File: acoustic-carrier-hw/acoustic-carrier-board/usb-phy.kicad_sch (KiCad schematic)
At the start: 52 parts, among them J801 TYPE-C-31-M-12, U801 USB3300-EZK, U802 LMV321, Y801 Crystal_GND24_Small

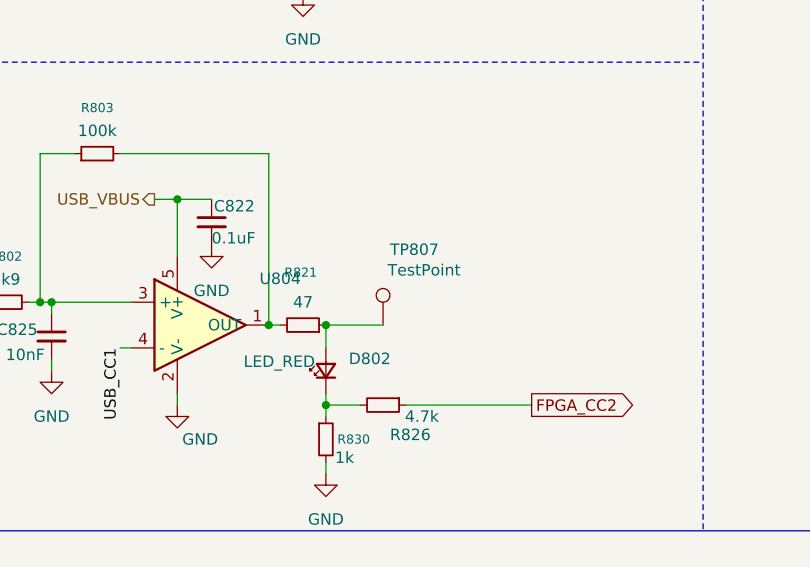
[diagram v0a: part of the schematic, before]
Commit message: [carrier] added silkscreen, moved lpddr3 traces around slightly
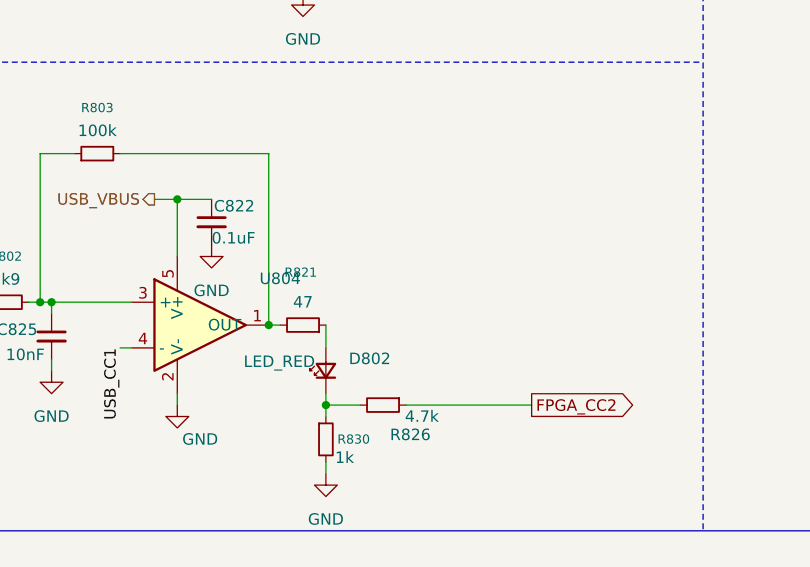
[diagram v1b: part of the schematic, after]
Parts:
- removed TP807: TestPoint, TestPoint:TestPoint_Loop_D1.80mm_Drill1.0mm_Beaded, symbol Connector:TestPoint
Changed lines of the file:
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@@
 	)
 	(junction
-		(at 288.29 224.79)
-		(diameter 0)
-		(color 0 0 0 0)
-	)
-	(junction
 		(at 279.4 172.72)
 		(diameter 0)
@@
 	(wire
 		(pts
-			(xy 288.29 224.79) (xy 294.64 224.79)
-		)
-		(stroke
-			(width 0)
-			(type default)
-		)
-	)
-	(wire
-		(pts
 			(xy 297.18 233.68) (xy 311.15 233.68)
 		)
@@
 					(unit 1)
 				)
-			)
-		)
-	)
-	(symbol
-		(lib_id "Connector:TestPoint")
-		(at 294.64 224.79 0)
-		(unit 1)
-		(exclude_from_sim no)
-		(in_bom yes)
-		(on_board yes)
-		(dnp no)
-		(property "Reference" "TP807"
-			(at 295.402 216.408 0)
-			(effects
-				(font
-					(size 1.27 1.27)
-				)
-				(justify left)
-			)
-		)
-		(property "Value" "TestPoint"
-			(at 295.148 218.694 0)
-			(effects
-				(font
-					(size 1.27 1.27)
-				)
-				(justify left)
-			)
-		)
-		(property "Footprint" "TestPoint:TestPoint_Loop_D1.80mm_Drill1.0mm_Beaded"
-			(at 299.72 224.79 0)
-			(effects
-				(font
-					(size 1.27 1.27)
-				)
-				(hide yes)
-			)
-		)
-		(property "Datasheet" "~"
-			(at 299.72 224.79 0)
-			(effects
-				(font
-					(size 1.27 1.27)
-				)
-				(hide yes)
-			)
-		)
-		(property "Description" "test point"
-			(at 294.64 224.79 0)
-			(effects
-				(font
-					(size 1.27 1.27)
-				)
-				(hide yes)
-			)
-		)
-		(pin "1"
-		)
-		(instances
-			(project "acoustic-carrier-board"
-				(path "/25b015c9-ab13-4427-b72c-b6f348597100/bccc7554-d2b1-4102-8d28-ddff56ec5c7a"
-					(reference "TP807")
-					(unit 1)
-				)

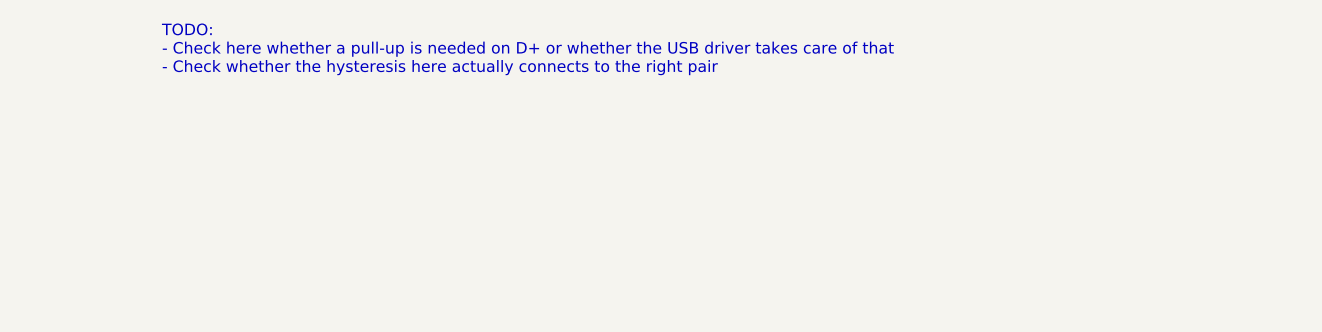
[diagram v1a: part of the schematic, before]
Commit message: [carrier] finished final review, (next) posting to linkedin, start working on analog front-end board
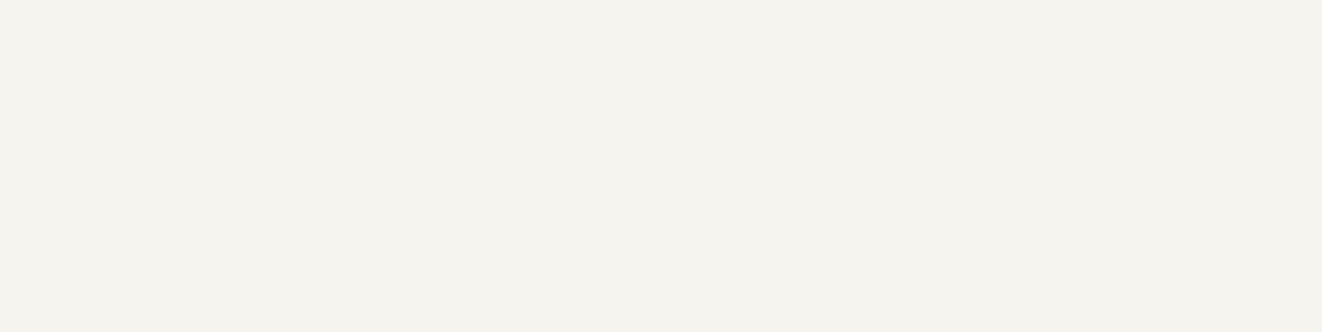
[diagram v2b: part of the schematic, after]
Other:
- note removed: "TODO: - Check here whether a pull-up is needed on D+ or whether the USB driver takes care of that - Check whether the hysteresis here actually connects to the right pair"
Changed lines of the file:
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@@
-		)
-	)
-	(text "TODO: \n- Check here whether a pull-up is needed on D+ or whether the USB driver takes care of that\n- Check whether the hysteresis here actually connects to the right pair"
-		(exclude_from_sim no)
-		(at 162.814 -21.336 0)
-		(effects
-			(font
-				(size 1.27 1.27)
-			)
-			(justify left bottom)
 		)
 	)

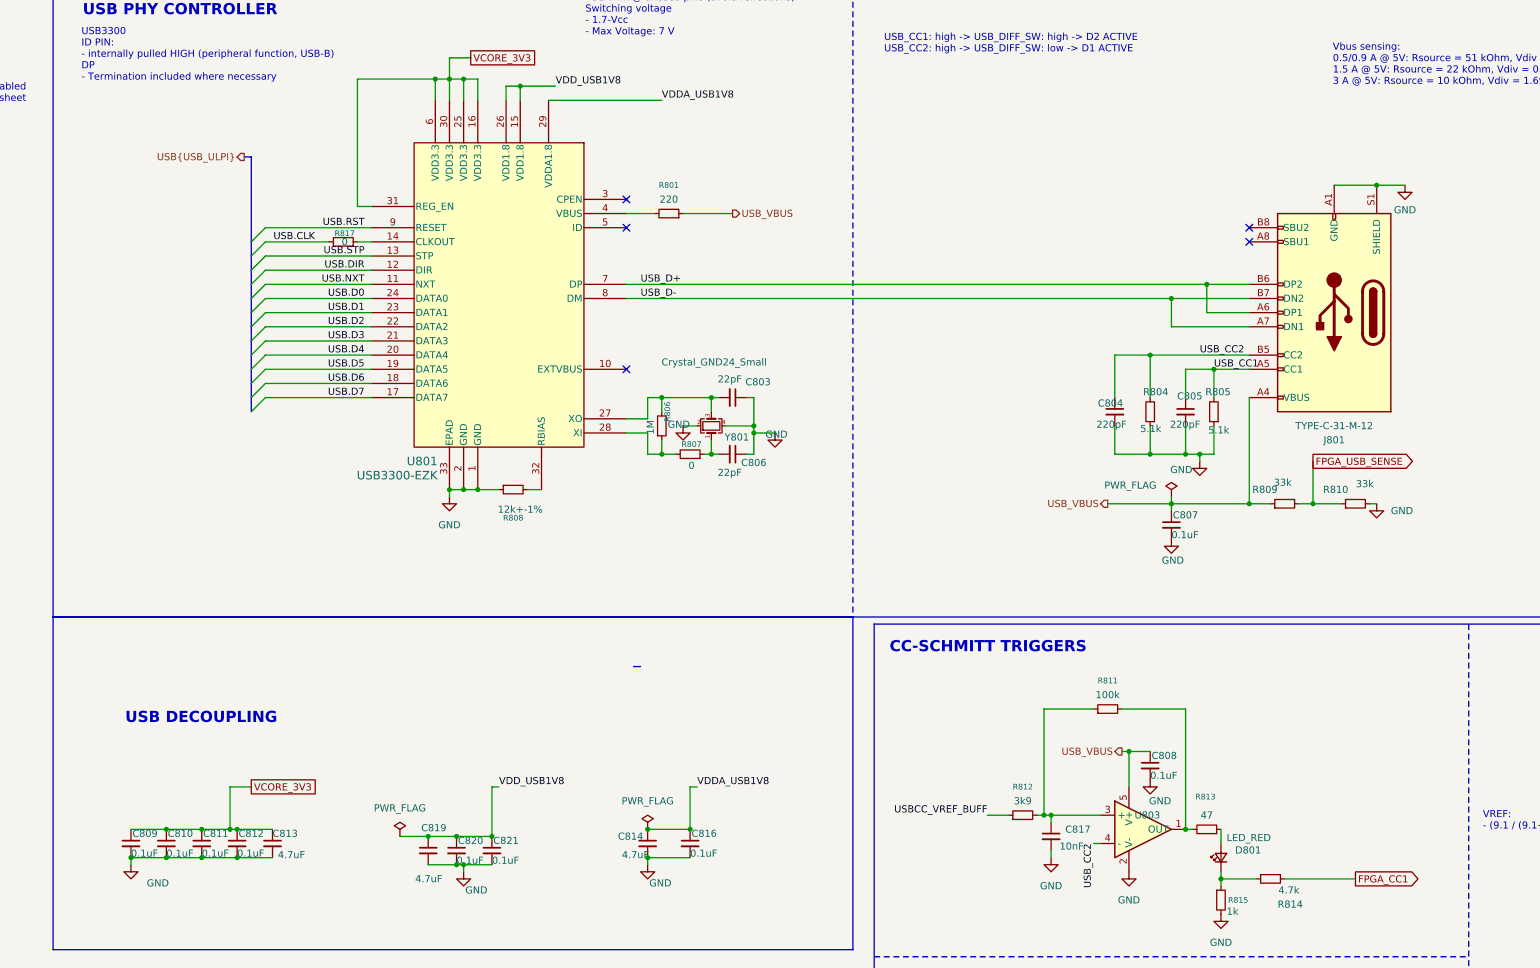
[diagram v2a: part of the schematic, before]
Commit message: [carrier] Added LC-filter between SHIELD and GND, added comments
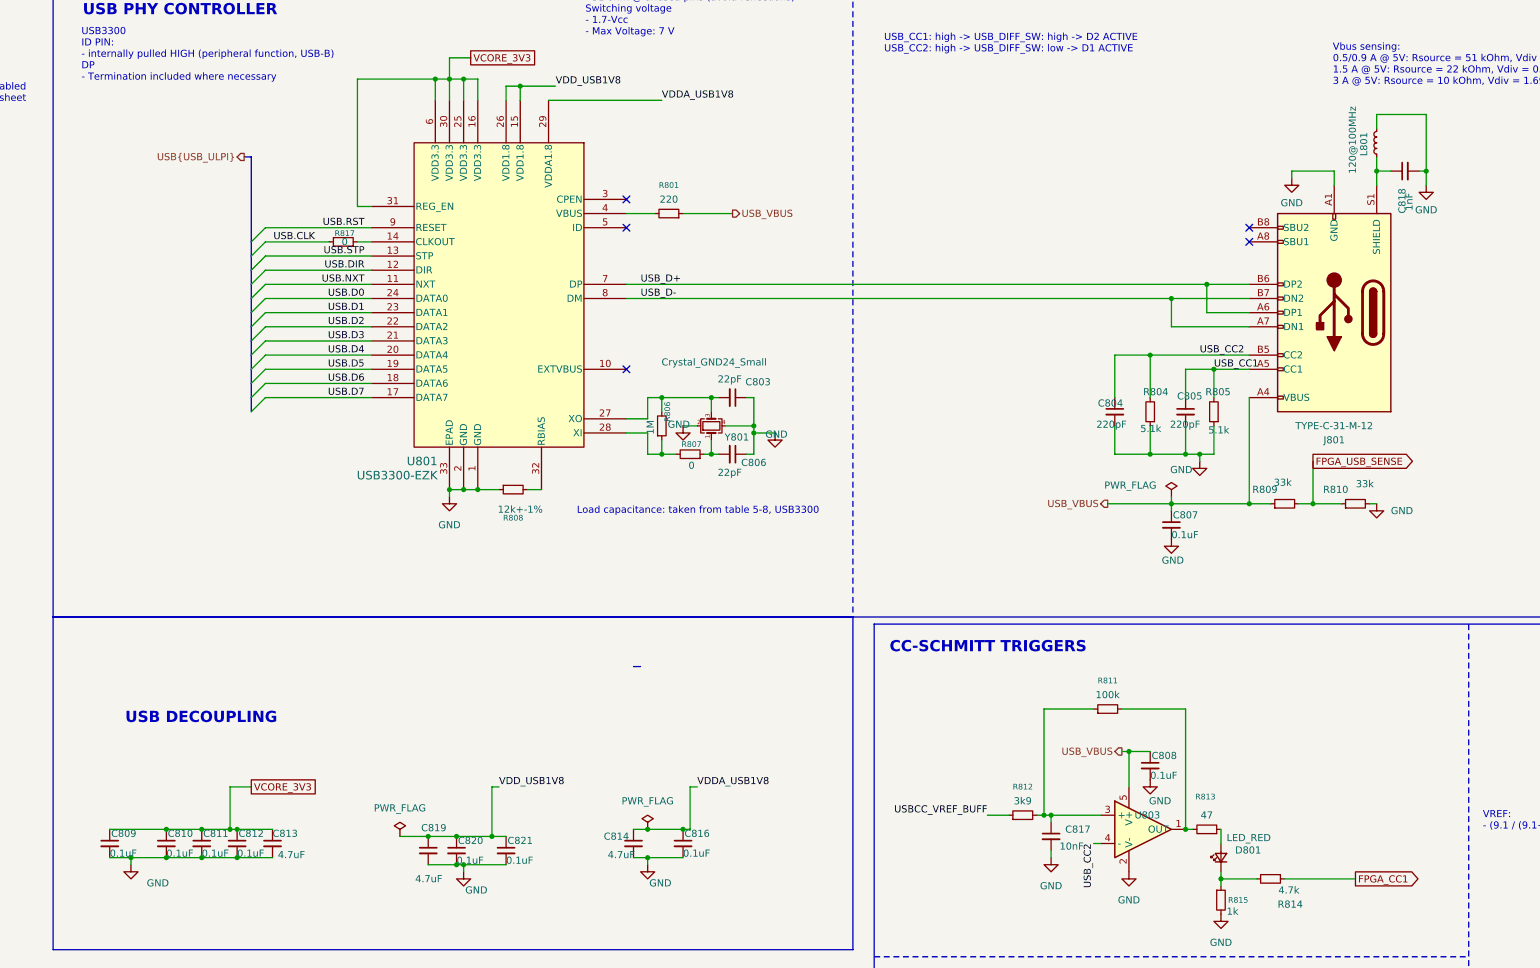
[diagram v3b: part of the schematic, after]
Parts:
- added C818: 1nF, Capacitor_SMD:C_1206_3216Metric, symbol Device:C_Small
- added L801: 120@100MHz, Inductor_SMD:L_0603_1608Metric, symbol Device:L_Small
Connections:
- net GND: now also C818.2, L801.1; no longer J801.S1 (SHIELD)
- new net: C818.1, J801.S1 (SHIELD), L801.2
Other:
- note added: "Load capacitance: taken from table 5-8, USB3300"
- moved on the sheet: C809, C814, C816, C821

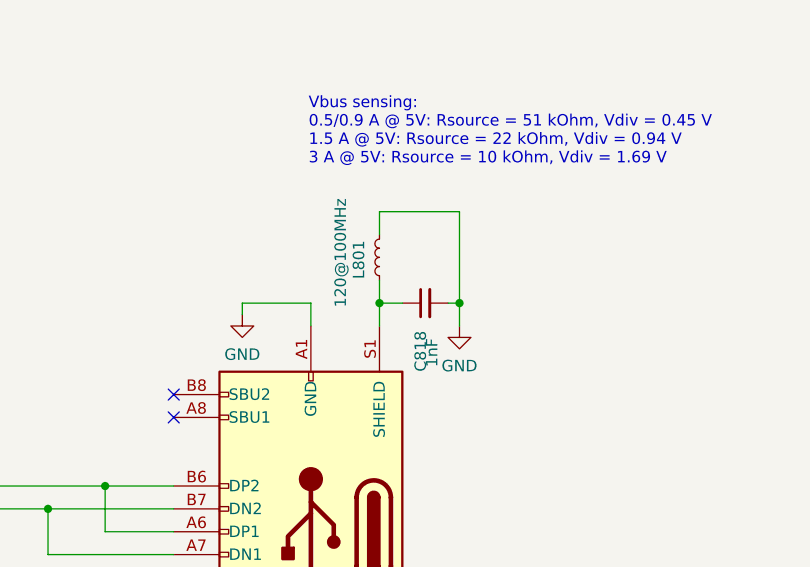
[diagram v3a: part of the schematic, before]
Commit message: [carrier] Added testpoints to lpddr3 (next) do final checks before ordering
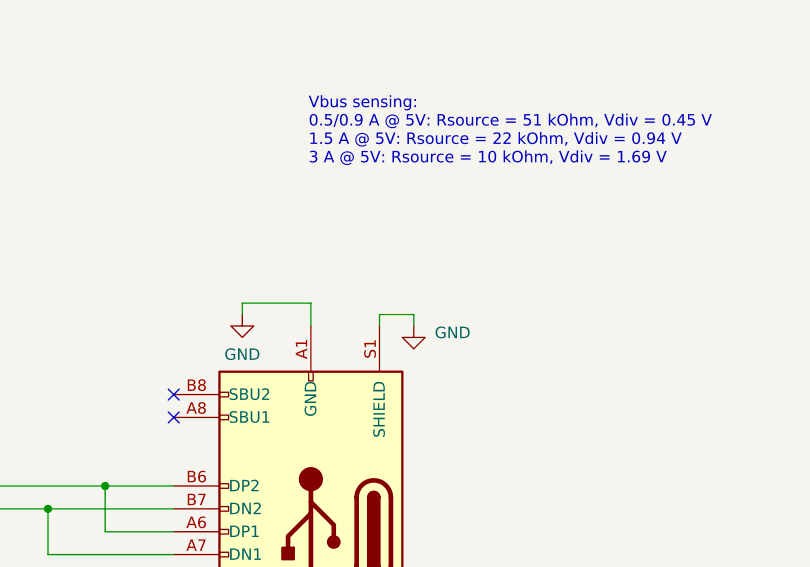
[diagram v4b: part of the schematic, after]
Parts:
- removed C818: 1nF, Capacitor_SMD:C_1206_3216Metric, symbol Device:C_Small
- removed L801: 120@100MHz, Inductor_SMD:L_0603_1608Metric, symbol Device:L_Small
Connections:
- net GND: now also J801.S1 (SHIELD)
